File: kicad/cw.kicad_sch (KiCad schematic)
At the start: 83 parts, among them J1 AUDIO, J2 KEY, Q1 NPN, Q2 NMOS, Q3 NPN, Q4 NPN, Q5 NPN, Q6 NPN, Q7 NPN, Q8 NPN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

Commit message: update schematic
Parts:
- removed SW1: FREQ, symbol Device:RotaryEncoder
- added C28, C29: C, symbol Device:C
- added L24, L25: L, symbol Device:L
- added Q10, Q11: NPN, symbol Simulation_SPICE:NPN
- added R10, R11: R, symbol Device:R
- added SW3: FREQ_SELECT, symbol Device:RotaryEncoder_Switch
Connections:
- net +12V: now also R1.2, C28.1, L24.2
- net +5V: now also C29.1, L25.2, SW3.S1
- net GND: now also Q10.3 (E), Q11.3 (E), R10.2, R11.2, SW3.C
- net at SW4.2 (B), U2.1 (VIN): no longer R1.2
- net at J2.S: now also C29.2, L25.1, Q11.1 (C); no longer U1.10 (CLK0)
- net at U1.6 (CLK2): now also Q10.2 (B), R10.1; no longer L16.2
- net at A1.7 (D4): now also SW3.S2
- net at A1.8 (D5): now also SW3.B
- net at A1.9 (D6): now also SW3.A
- new net: Q11.2 (B), R11.1, U1.10 (CLK0)
- new net: C28.2, L16.2, L24.1, Q10.1 (C)
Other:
- moved on the sheet: C1, C12, C18, C19, C22, C23, D4, J2, L1, L13, L15, L16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

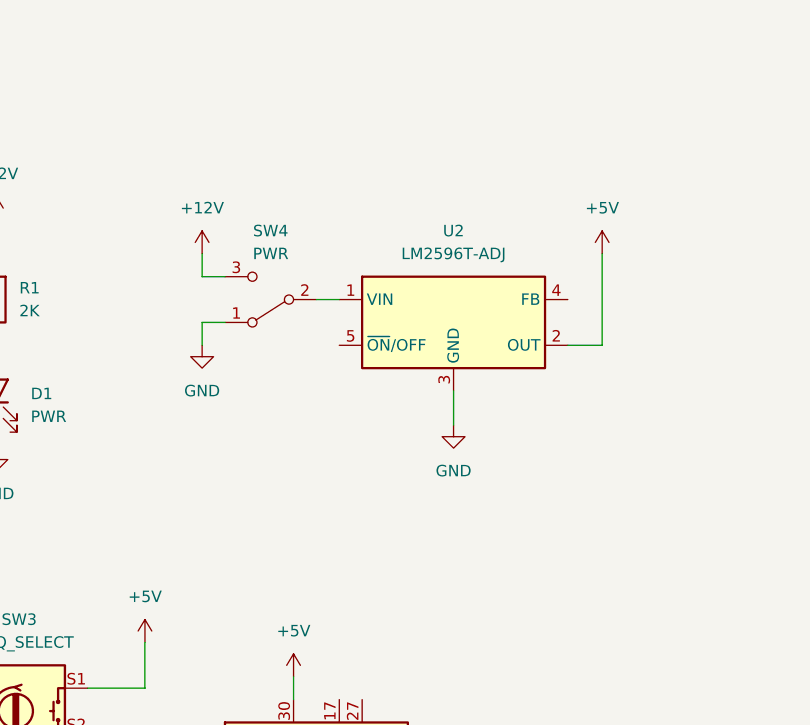
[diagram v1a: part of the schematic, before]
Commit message: add fuse
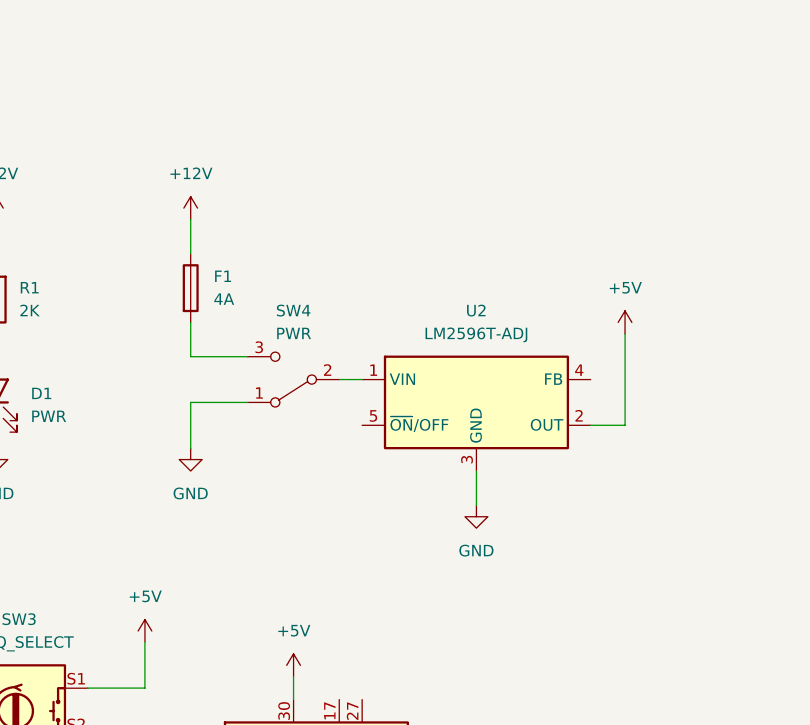
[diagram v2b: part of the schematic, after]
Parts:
- added F1: 4A, symbol Device:Fuse
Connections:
- net +12V: now also F1.1; no longer SW4.3 (C)
- new net: F1.2, SW4.3 (C)
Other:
- moved on the sheet: SW4, U2
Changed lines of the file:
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@@
     (stroke (width 0) (type default))
   )
-  (wire (pts (xy 69.85 91.44) (xy 72.39 91.44))
+  (wire (pts (xy 72.39 100.33) (xy 74.93 100.33))
     (stroke (width 0) (type default))
   )
@@
     (stroke (width 0) (type default))
   )
-  (wire (pts (xy 57.15 86.36) (xy 57.15 88.9))
+  (wire (pts (xy 55.88 82.55) (xy 55.88 86.36))
     (stroke (width 0) (type default))
   )
@@
     (stroke (width 0) (type default))
   )
-  (wire (pts (xy 85.09 105.41) (xy 85.09 101.6))
+  (wire (pts (xy 87.63 114.3) (xy 87.63 110.49))
     (stroke (width 0) (type default))
   )
@@
     (stroke (width 0) (type default))
   )
-  (wire (pts (xy 57.15 93.98) (xy 59.69 93.98))
+  (wire (pts (xy 55.88 102.87) (xy 62.23 102.87))
     (stroke (width 0) (type default))
   )
@@
     (stroke (width 0) (type default))
   )
+  (wire (pts (xy 55.88 93.98) (xy 55.88 97.79))
+    (stroke (width 0) (type default))
+  )
   (wire (pts (xy 237.49 298.45) (xy 237.49 299.72))
     (stroke (width 0) (type default))
@@
     (stroke (width 0) (type default))
   )
-  (wire (pts (xy 97.79 96.52) (xy 101.6 96.52))
+  (wire (pts (xy 100.33 105.41) (xy 104.14 105.41))
     (stroke (width 0) (type default))
   )
@@
     (stroke (width 0) (type default))
   )
-  (wire (pts (xy 57.15 96.52) (xy 57.15 93.98))
+  (wire (pts (xy 55.88 107.95) (xy 55.88 102.87))
     (stroke (width 0) (type default))
   )
@@
     (stroke (width 0) (type default))
   )
-  (wire (pts (xy 101.6 96.52) (xy 101.6 86.36))
+  (wire (pts (xy 104.14 105.41) (xy 104.14 95.25))
     (stroke (width 0) (type default))
   )
@@
     (stroke (width 0) (type default))
   )
-  (wire (pts (xy 57.15 88.9) (xy 59.69 88.9))
+  (wire (pts (xy 55.88 97.79) (xy 62.23 97.79))
     (stroke (width 0) (type default))
   )
@@
     )
   )
-  (symbol (lib_id "Regulator_Switching:LM2596T-ADJ") (at 85.09 93.98 0) (unit 1)
+  (symbol (lib_id "Regulator_Switching:LM2596T-ADJ") (at 87.63 102.87 0) (unit 1)
     (in_bom yes) (on_board yes) (dnp no) (fields_autoplaced)
-    (property "Reference" "U2" (at 85.09 83.82 0)
+    (property "Reference" "U2" (at 87.63 92.71 0)
       (effects (font (size 1.27 1.27)))
     )
-    (property "Value" "LM2596T-ADJ" (at 85.09 86.36 0)
+    (property "Value" "LM2596T-ADJ" (at 87.63 95.25 0)
       (effects (font (size 1.27 1.27)))
     )
-    (property "Footprint" "Package_TO_SOT_THT:TO-220-5_P3.4x3.7mm_StaggerOdd_Lead3.8mm_Vertical" (at 86.36 100.33 0)
+    (property "Footprint" "Package_TO_SOT_THT:TO-220-5_P3.4x3.7mm_StaggerOdd_Lead3.8mm_Vertical" (at 88.9 109.22 0)
       (effects (font (size 1.27 1.27) italic) (justify left) hide)
     )
-    (property "Datasheet" "http://www.ti.com/lit/ds/symlink/lm2596.pdf" (at 85.09 93.98 0)
+    (property "Datasheet" "http://www.ti.com/lit/ds/symlink/lm2596.pdf" (at 87.63 102.87 0)
       (effects (font (size 1.27 1.27)) hide)
     )
@@
     )
   )
-  (symbol (lib_id "power:+12V") (at 57.15 86.36 0) (unit 1)
+  (symbol (lib_id "power:+12V") (at 55.88 82.55 0) (unit 1)
     (in_bom yes) (on_board yes) (dnp no) (fields_autoplaced)
-    (property "Reference" "#PWR03" (at 57.15 90.17 0)
+    (property "Reference" "#PWR03" (at 55.88 86.36 0)
       (effects (font (size 1.27 1.27)) hide)
     )
-    (property "Value" "+12V" (at 57.15 81.28 0)
+    (property "Value" "+12V" (at 55.88 77.47 0)
       (effects (font (size 1.27 1.27)))
     )
-    (property "Footprint" "" (at 57.15 86.36 0)
+    (property "Footprint" "" (at 55.88 82.55 0)
       (effects (font (size 1.27 1.27)) hide)
     )
-    (property "Datasheet" "" (at 57.15 86.36 0)
+    (property "Datasheet" "" (at 55.88 82.55 0)
       (effects (font (size 1.27 1.27)) hide)
     )
@@
     )
   )
-  (symbol (lib_id "power:GND") (at 85.09 105.41 0) (unit 1)
+  (symbol (lib_id "power:GND") (at 87.63 114.3 0) (unit 1)
     (in_bom yes) (on_board yes) (dnp no) (fields_autoplaced)
-    (property "Reference" "#PWR04" (at 85.09 111.76 0)
+    (property "Reference" "#PWR04" (at 87.63 120.65 0)
       (effects (font (size 1.27 1.27)) hide)
     )
-    (property "Value" "GND" (at 85.09 110.49 0)
+    (property "Value" "GND" (at 87.63 119.38 0)
       (effects (font (size 1.27 1.27)))
     )
-    (property "Footprint" "" (at 85.09 105.41 0)
+    (property "Footprint" "" (at 87.63 114.3 0)
       (effects (font (size 1.27 1.27)) hide)
     )
-    (property "Datasheet" "" (at 85.09 105.41 0)
+    (property "Datasheet" "" (at 87.63 114.3 0)
       (effects (font (size 1.27 1.27)) hide)
     )
@@
     )
   )
-  (symbol (lib_id "power:+5V") (at 101.6 86.36 0) (unit 1)
+  (symbol (lib_id "power:+5V") (at 104.14 95.25 0) (unit 1)
     (in_bom yes) (on_board yes) (dnp no) (fields_autoplaced)
-    (property "Reference" "#PWR05" (at 101.6 90.17 0)
+    (property "Reference" "#PWR05" (at 104.14 99.06 0)
       (effects (font (size 1.27 1.27)) hide)
     )
-    (property "Value" "+5V" (at 101.6 81.28 0)
+    (property "Value" "+5V" (at 104.14 90.17 0)
       (effects (font (size 1.27 1.27)))
     )
-    (property "Footprint" "" (at 101.6 86.36 0)
+    (property "Footprint" "" (at 104.14 95.25 0)
       (effects (font (size 1.27 1.27)) hide)
     )
-    (property "Datasheet" "" (at 101.6 86.36 0)
+    (property "Datasheet" "" (at 104.14 95.25 0)
       (effects (font (size 1.27 1.27)) hide)
     )
@@
     )
   )
-  (symbol (lib_id "power:GND") (at 57.15 96.52 0) (unit 1)
+  (symbol (lib_id "power:GND") (at 55.88 107.95 0) (unit 1)
     (in_bom yes) (on_board yes) (dnp no) (fields_autoplaced)
-    (property "Reference" "#PWR014" (at 57.15 102.87 0)
+    (property "Reference" "#PWR014" (at 55.88 114.3 0)
       (effects (font (size 1.27 1.27)) hide)
     )
-    (property "Value" "GND" (at 57.15 101.6 0)
+    (property "Value" "GND" (at 55.88 113.03 0)
       (effects (font (size 1.27 1.27)))
     )
-    (property "Footprint" "" (at 57.15 96.52 0)
+    (property "Footprint" "" (at 55.88 107.95 0)
       (effects (font (size 1.27 1.27)) hide)
     )
-    (property "Datasheet" "" (at 57.15 96.52 0)
+    (property "Datasheet" "" (at 55.88 107.95 0)
       (effects (font (size 1.27 1.27)) hide)
     )
@@
     )
   )
-  (symbol (lib_id "Switch:SW_SPDT") (at 64.77 91.44 180) (unit 1)
+  (symbol (lib_id "Switch:SW_SPDT") (at 67.31 100.33 180) (unit 1)
     (in_bom yes) (on_board yes) (dnp no) (fields_autoplaced)
-    (property "Reference" "SW4" (at 64.77 83.82 0)
+    (property "Reference" "SW4" (at 67.31 92.71 0)
       (effects (font (size 1.27 1.27)))
     )
-    (property "Value" "PWR" (at 64.77 86.36 0)
+    (property "Value" "PWR" (at 67.31 95.25 0)
       (effects (font (size 1.27 1.27)))
     )
-    (property "Footprint" "" (at 64.77 91.44 0)
+    (property "Footprint" "" (at 67.31 100.33 0)
       (effects (font (size 1.27 1.27)) hide)
     )
-    (property "Datasheet" "~" (at 64.77 91.44 0)
+    (property "Datasheet" "~" (at 67.31 100.33 0)
       (effects (font (size 1.27 1.27)) hide)
     )
@@
         )
       )
+    )
+  )
+  (symbol (lib_id "Device:Fuse") (at 55.88 90.17 0) (unit 1)
+    (in_bom yes) (on_board yes) (dnp no) (fields_autoplaced)
+    (property "Reference" "F1" (at 58.42 88.9 0)
+      (effects (font (size 1.27 1.27)) (justify left))
+    )
+    (property "Value" "4A" (at 58.42 91.44 0)
+      (effects (font (size 1.27 1.27)) (justify left))
+    )
+    (property "Footprint" "" (at 54.102 90.17 90)
+      (effects (font (size 1.27 1.27)) hide)
+    )
+    (property "Datasheet" "~" (at 55.88 90.17 0)
+      (effects (font (size 1.27 1.27)) hide)
+    )
+    (pin "1")
+    (pin "2")
+    (instances
+      (project "cw"
+        (path "/817248d0-f027-4dd0-8ccd-515a582be88c"
+          (reference "F1") (unit 1)
+        )
+      )

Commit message: Update cw.kicad_sch
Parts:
- removed SW4: PWR, symbol Switch:SW_SPDT
- removed U2: LM2596T-ADJ, Package_TO_SOT_THT:TO-220-5_P3.4x3.7mm_StaggerOdd_Lead3.8mm_Vertical, symbol Regulator_Switching:LM2596T-ADJ
- added BT1: Battery, symbol Device:Battery
- added SW1: TX/RX, symbol Switch:SW_SPDT
- F1: value 4A -> Fuse
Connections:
- net +12V: now also A1.30 (VIN), F1.2; no longer F1.1
- net +5V: no longer A1.30 (VIN), SW3.S1, U1.1 (VDD), U3.5 (VDD), U4.2 (VDD)
- net GND: now also BT1.2 (-)
- net at A1.17 (3V3): now also U1.1 (VDD), U3.5 (VDD), U4.2 (VDD)
- net at A1.27 (+5V): now also SW3.S1
- new net: F1.1, SW1.2 (B)
- new net: BT1.1 (+), SW1.3 (C)
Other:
- moved on the sheet: D1, R1

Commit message: Update cw.kicad_sch
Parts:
- removed C13, C24, C25, C28, C29: C, symbol Device:C
- removed L21, L22, L24, L25, L9: L, symbol Device:L
- removed Q8, Q9: NPN, symbol Simulation_SPICE:NPN
- removed R9: R, symbol Device:R
- added Q12, Q13: NPN, symbol Simulation_SPICE:NPN
- added R12, R13, R14, R15, R16, R17, R18, R19, R20, R21, R22: R, symbol Device:R
- BT1: value Battery -> 12V
- F1: value Fuse -> 4A
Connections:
- net +12V: now also Q10.1 (C), Q11.1 (C), Q7.1 (C), R10.1, R7.1, Q12.1 (C), Q13.1 (C), R13.1, R14.1, R19.1
- net GND: now also R12.2, R15.2, R16.2, R17.2, R18.2, R20.2, R21.2, R22.2; no longer Q10.3 (E), Q11.3 (E), Q7.3 (E), R10.2, R7.2
- net at C12.2, Q5.2 (B), R4.1: now also Q7.2 (B), R7.2, R8.1
- net at C2.2, Q3.2 (B), R3.1: now also Q7.3 (E), R22.1
- net at L23.1: now also Q10.3 (E), R18.1; no longer Q7.1 (C)
- net at J2.S: now also Q11.3 (E), R12.1; no longer Q11.1 (C)
- net at Q11.2 (B), R11.1, U1.10 (CLK0): now also R13.2
- net at L11.1: now also Q13.3 (E), R21.1
- net at L16.2: now also Q12.3 (E), R16.1; no longer Q10.1 (C)
- new net: Q12.2 (B), R14.2, R15.1, U1.6 (CLK2)
- new net: Q10.2 (B), Q13.2 (B), R10.2, R17.1, R19.2, R20.1, U1.9 (CLK1)
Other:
- moved on the sheet: BT1, C18, C19, C22, C23, C26, D1, D4, F1, L13, L15, L16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

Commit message: Update cw.kicad_sch
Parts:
- removed Q12, Q13: NPN, symbol Simulation_SPICE:NPN
- removed R17, R18, R19, R20, R21, R22: R, symbol Device:R
- added C13, C24, C25, C28, C29: C, symbol Device:C
- added Q8, Q9: NPN, symbol Simulation_SPICE:NPN
- added R9: R, symbol Device:R
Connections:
- net +12V: now also Q8.1 (C), Q9.1 (C); no longer R10.1, R13.1, R14.1, R7.1
- net GND: now also R10.2, R13.2, R14.2, R7.2, R9.2
- net at C12.2, Q5.2 (B), R4.1: now also C29.1; no longer Q7.2 (B), R7.2, R8.1
- net at C2.2, Q3.2 (B), R3.1: now also Q10.3 (E), R16.1; no longer Q7.3 (E)
- net at L23.1: now also Q7.3 (E), R8.1; no longer Q10.3 (E)
- net at L16.2: now also R13.1, Q8.3 (E); no longer R16.1
- net at Q11.2 (B), R11.1: now also C13.2; no longer R13.2, U1.10 (CLK0)
- net at L11.1: now also R14.1, Q9.3 (E)
- new net: C24.1, U1.6 (CLK2)
- new net: C24.2, Q8.2 (B), R9.1
- new net: C29.2, Q10.2 (B), R15.1
- new net: C13.1, U1.10 (CLK0)
- new net: C25.1, C28.1, U1.9 (CLK1)
- new net: C25.2, Q7.2 (B), R7.1
- new net: C28.2, Q9.2 (B), R10.1
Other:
- moved on the sheet: Q11, R11, R12
